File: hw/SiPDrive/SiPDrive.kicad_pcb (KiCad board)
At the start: 8 copper layers, 23 x 27.5 mm, 62 parts, among them Q1 CMSA015N06, Q2 CMSA015N06, Q3 CMSA015N06, Q4 CMSA015N06, Q5 CMSA015N06, Q6 CMSA015N06, U1 STSPIN32G4, U2 MT6701, U3 TCAN1057, U4 LDO, U5 SH-3P

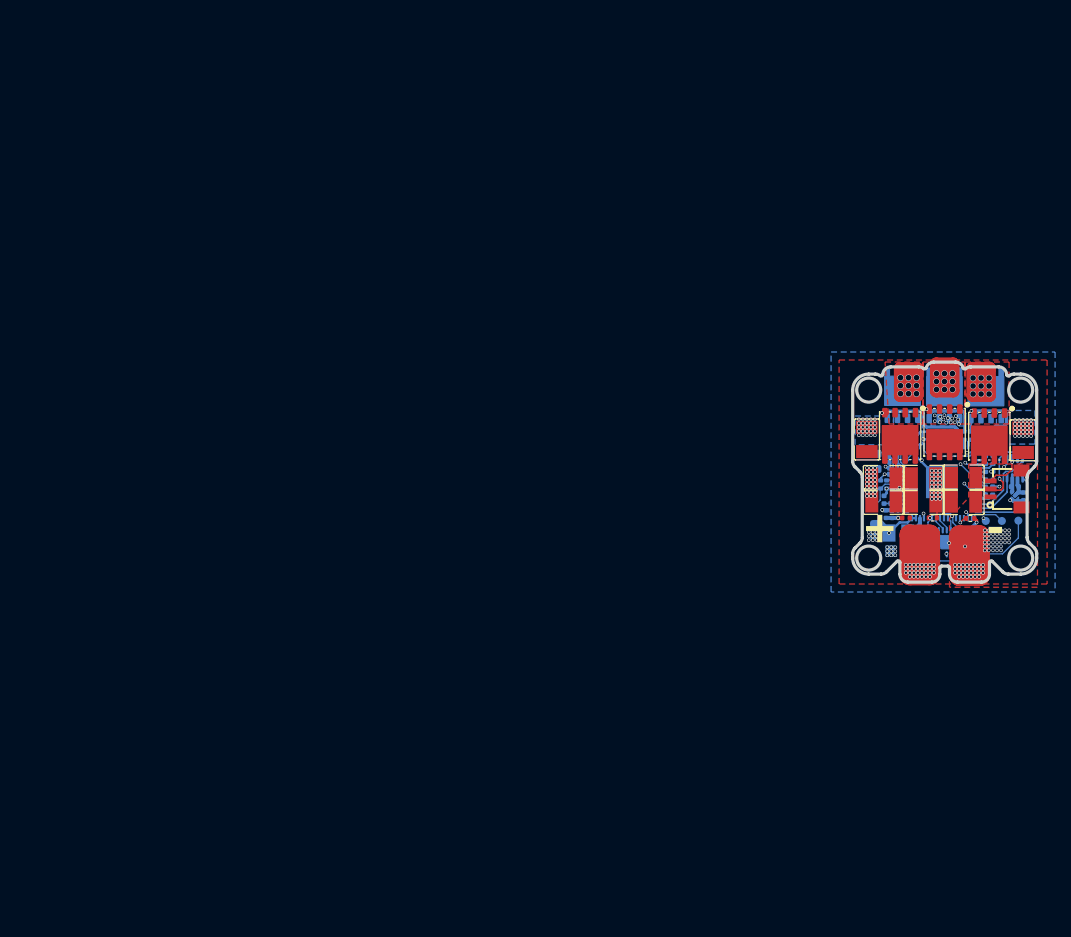
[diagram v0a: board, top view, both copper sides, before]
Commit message: Updated schematic to a 3 shunt topology and made first deboard PCB layout
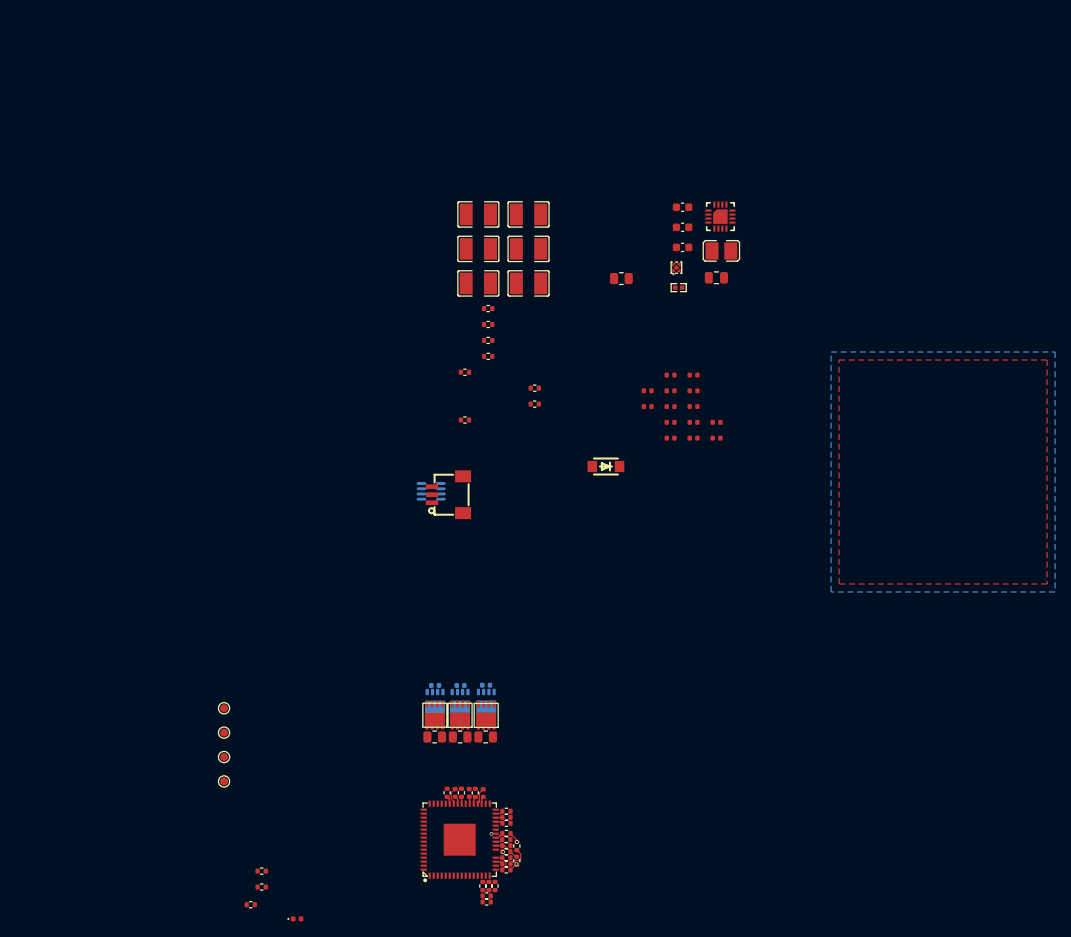
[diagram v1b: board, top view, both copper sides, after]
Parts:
- removed C24, C26: 10uF, SiPDrive:C1210
- added C27: 1uF, Capacitor_SMD:C_0402_1005Metric, B.Cu at (92.9, 125.7)
- added C28: 1uF, Capacitor_SMD:C_0402_1005Metric, B.Cu at (86.5, 125.7)
- added C29: 1uF, Capacitor_SMD:C_0402_1005Metric, B.Cu at (89.7, 125.7)
- added C30: 33n, Capacitor_SMD:C_0402_1005Metric, F.Cu at (121.7, 92.8)
- added C31: 1uF, Capacitor_SMD:C_0603_1608Metric, F.Cu at (117.4, 70.9)
- added C8: 100n, Capacitor_SMD:C_0402_1005Metric, F.Cu at (115.9, 88.9)
- added R20: 1mR, Resistor_SMD:R_0805_2012Metric, F.Cu at (86.5, 132.1)
- added R21: 120R, Resistor_SMD:R_0805_2012Metric, F.Cu at (109.8, 74.8)
- added R22: 1.5k, Resistor_SMD:R_0402_1005Metric, F.Cu at (92.5, 150.8)
- added R23: 1.5k, Resistor_SMD:R_0402_1005Metric, F.Cu at (93.2, 150.8)
- added R24: 15k, Resistor_SMD:R_0402_1005Metric, F.Cu at (94.0, 150.8)
- added R25: 30k, Resistor_SMD:R_0402_1005Metric, F.Cu at (93.0, 152.0)
- added R26: 30k, Resistor_SMD:R_0402_1005Metric, F.Cu at (93.0, 152.8)
- added R27: 15k, Resistor_SMD:R_0402_1005Metric, F.Cu at (95.4, 144.9)
- added R28: 1.5k, Resistor_SMD:R_0402_1005Metric, F.Cu at (95.4, 145.7)
- added R29: 1.5k, Resistor_SMD:R_0402_1005Metric, F.Cu at (95.4, 144.2)
- added R30: 30k, Resistor_SMD:R_0402_1005Metric, F.Cu at (96.7, 147.6)
- added R31: 30k, Resistor_SMD:R_0402_1005Metric, F.Cu at (95.4, 146.5)
- added R32: 15k, Resistor_SMD:R_0402_1005Metric, F.Cu at (95.4, 148.0)
- added R33: 1.5k, Resistor_SMD:R_0402_1005Metric, F.Cu at (95.4, 147.2)
- added R34: 1.5k, Resistor_SMD:R_0402_1005Metric, F.Cu at (96.7, 145.8)
- added R35: 30k, Resistor_SMD:R_0402_1005Metric, F.Cu at (95.4, 148.7)
- added R36: 30k, Resistor_SMD:R_0402_1005Metric, F.Cu at (99.0, 88.5)
- added R37: 10k, Resistor_SMD:R_0402_1005Metric, F.Cu at (99.0, 90.5)
- C1, C10, C11, C12, C13, C14, C15, C16, C17, C2, C3, C4, C5, C6, C9, D1, D2, FB1, L1, R11, R12, R13, R14, R16, R18, R2, R3, R4, R5, R6, R7, R8, R9, TP1, TP2, TP3, TP4, U1, U2, U4: moved to F.Cu
- C7: value 100n -> 220n; footprint Capacitor_SMD:C_0402_1005Metric -> Capacitor_SMD:C_0603_1608Metric
- Q1, Q3, Q5: value CMSA015N06 -> SP40N03GNJ; footprint SiPDrive:PDFN-8_L5.8-W5.0-P1.27-LS6.1-BL -> SiPDrive:POWERPAK-1212-8_L3.0-W3.0-P0.65-LS3.3-BL; moved to B.Cu
- Q2, Q4, Q6: value CMSA015N06 -> SP40N03GNJ; footprint SiPDrive:PDFN-8_L5.8-W5.0-P1.27-LS6.1-BL -> SiPDrive:POWERPAK-1212-8_L3.0-W3.0-P0.65-LS3.3-BL; moved to F.Cu
- R1, R19: value HOSRX -> 1mR; footprint SiPDrive:RES-SMD_L3.2-W1.6_SR120620F0M50SZ -> Resistor_SMD:R_0805_2012Metric; moved to F.Cu
- R10: value 200k -> 100k; moved to F.Cu
- R15: value 10k -> 100k
- moved TP4 104.5 mm to (60.1, 137.7), turned to 0 degrees
- moved TP2 100.8 mm to (60.1, 131.6), turned to 0 degrees
- moved TP1 98.1 mm to (60.1, 128.5), turned to 0 degrees
- moved R17 94.8 mm to (64.8, 148.9)
- moved R16 94.6 mm to (63.5, 153.1), turned to 0 degrees
- moved R18 92.5 mm to (64.8, 150.9), turned to 0 degrees
- moved D2 90.2 mm to (69.3, 154.9), turned to 0 degrees
- moved TP3 86.8 mm to (60.1, 134.6)
- moved R2 78.0 mm to (88.0, 139.1)
- moved R4 77.4 mm to (89.8, 139.1)
- moved R7 77.0 mm to (91.5, 139.1)
- moved C1 76.3 mm to (89.0, 139.1), turned to 90 degrees
- moved C4 75.8 mm to (90.8, 139.1), turned to 90 degrees
- moved C5 75.4 mm to (92.5, 139.1), turned to 90 degrees
- moved U1 75.0 mm to (89.6, 145.0), turned to 90 degrees
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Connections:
- Q4 pad 3: GND -> Net-(Q4-S)
- R1 pad 2: Net-(Q2-S) -> Net-(Q4-S)
- R6 pad 1: /ENC_MODE -> Net-(JP1-B)
- U1 pad 14: Net-(Q2-S) -> Net-(U1-PA1)
- U1 pad 16: GND -> Net-(U1-PA3)
- U1 pad 18: GND -> unconnected-(U1-PA5-Pad18)
- U1 pad 19: unconnected-(U1-PA6-Pad19) -> Net-(U1-PA6)
- U1 pad 20: Net-(Q6-S) -> Net-(U1-PA7)
- U1 pad 23: unconnected-(U1-PB0-Pad23) -> Net-(U1-PB0)
- U1 pad 56: /ENC_MODE -> unconnected-(U1-PB5-Pad56)
- U2 pad 14: /ENC_MODE -> Net-(JP1-B)
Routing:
- net GND: track 32.3 -> 1.54 mm, vias 205 -> 2
- net +12V: track 25.8 -> 0.00 mm, vias 2 -> 0
- net Net-(Q1-G): track 20.4 -> 0.00 mm, vias 2 -> 0
- net /BOOT0: track 19.3 -> 0.00 mm, vias 1 -> 0
- net +3.3V: track 20.8 -> 1.73 mm, vias 5 -> 2
- net /PhaseU: track 19.0 -> 2.14 mm, vias 10 -> 0
- net /PhaseV: track 14.2 -> 0.00 mm, vias 10 -> 0
- net Net-(Q3-G): track 12.8 -> 0.00 mm, vias 2 -> 0
- net /PhaseW: track 14.1 -> 2.09 mm, vias 10 -> 0
- net Net-(Q2-G): track 11.5 -> 0.00 mm
- net Net-(Q5-G): track 11.1 -> 0.00 mm, vias 1 -> 0
- net /CAN_TX: track 10.0 -> 0.00 mm
- net Net-(Q6-S): track 9.59 -> 0.00 mm
- net /CAN_EN: track 9.33 -> 0.00 mm
- net /ENC_MODE: track 8.96 -> 0.00 mm, vias 2 -> 0
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- removed copper zone on F.Cu, net /PhaseU
- removed copper zone on F.Cu, net /PhaseV
- removed copper zone on F.Cu, net /PhaseW
- removed copper zone on F.Cu, net GND
- removed copper zone on B.Cu, net Net-(Q2-S)
- removed copper zone on B.Cu, net Net-(Q6-S)
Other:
- board outline removed
- board text removed: "+"
- board text removed: "-"
- board text removed: "3S-12S"
- board text removed: "mini"
- board text removed: "moteus"

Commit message: Ordered first dev board and components
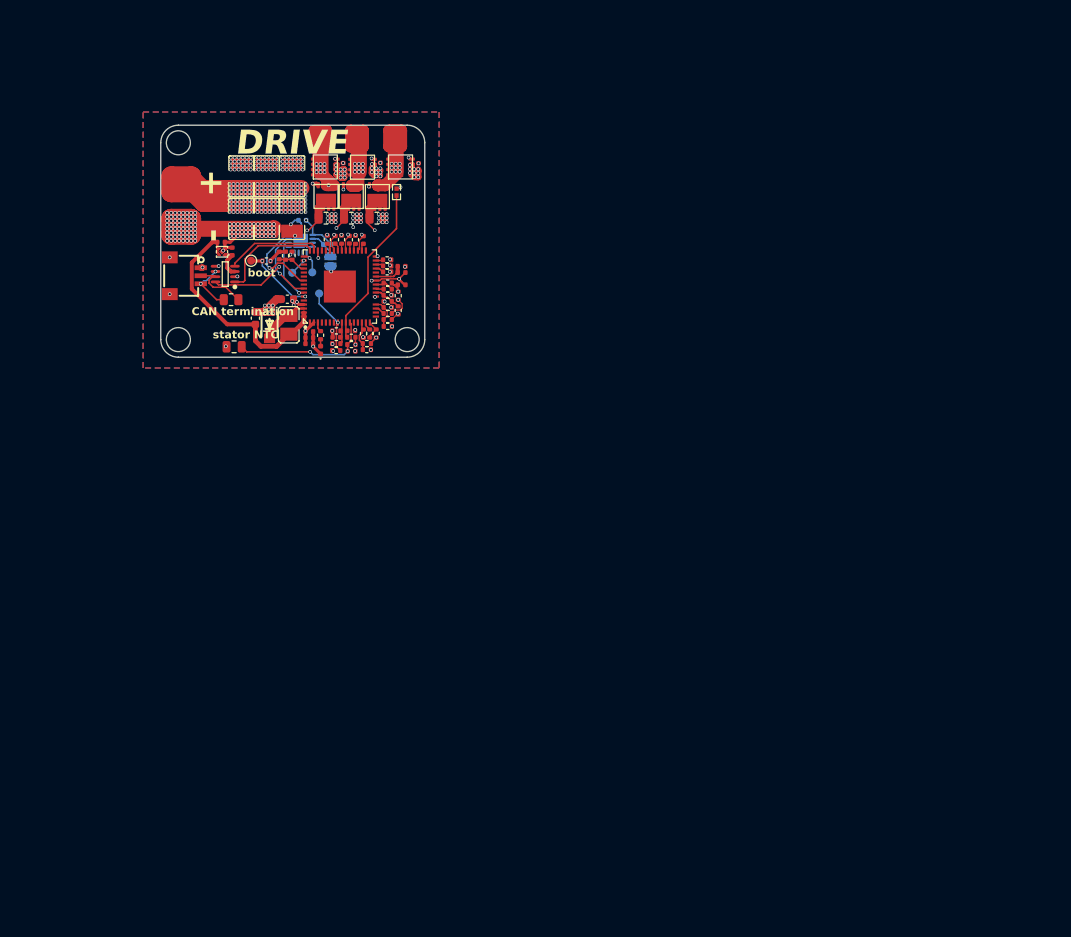
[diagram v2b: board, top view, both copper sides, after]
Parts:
- removed C3, C8: 100n, Capacitor_SMD:C_0402_1005Metric
- added JP1: jmpOpen1, Jumper:SolderJumper-2_P1.3mm_Open_RoundedPad1.0x1.5mm, B.Cu at (73.4, 72.7)
- C12, R6, TP1, TP2, TP3, U2: moved to B.Cu
- C27, C28, C29, Q1, Q3, Q5, U3: moved to F.Cu
- C31: footprint Capacitor_SMD:C_0603_1608Metric -> Capacitor_SMD:C_0402_1005Metric
- moved R17 76.3 mm to (65.4, 72.6)
- moved D2 71.2 mm to (72.2, 83.8), turned to 90 degrees
- moved R24 70.8 mm to (78.3, 81.7)
- moved C1 70.7 mm to (74.0, 70.0)
- moved C4 70.7 mm to (75.8, 70.0)
- moved R7 70.7 mm to (76.5, 70.0)
- moved U1 70.7 mm to (74.6, 75.8)
- moved R2 70.7 mm to (73.0, 70.0)
- moved R4 70.7 mm to (74.8, 70.0)
- moved C5 70.7 mm to (77.5, 70.0)
- moved R25 70.7 mm to (78.0, 82.9)
- moved R26 70.7 mm to (78.0, 83.7)
- moved R22 70.6 mm to (77.5, 81.7)
- moved R3 70.5 mm to (80.5, 74.0)
- moved R5 70.5 mm to (80.5, 73.2)
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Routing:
- net +BATT: track 0.00 -> 65.6 mm, vias 0 -> 191
- net GND: track 1.54 -> 42.2 mm, vias 2 -> 249
- net +12V: track 0.00 -> 29.8 mm
- net Net-(Q2-S): track 0.00 -> 21.1 mm, vias 0 -> 2
- net /BOARD_NTC: track 0.00 -> 20.4 mm
- net Net-(Q4-S): track 0.00 -> 19.2 mm, vias 0 -> 2
- net Net-(Q2-G): track 0.00 -> 18.8 mm, vias 0 -> 2
- net /PhaseW: track 2.09 -> 20.4 mm, vias 0 -> 10
- net /PhaseV: track 0.00 -> 17.9 mm, vias 0 -> 10
- net Net-(Q4-G): track 0.00 -> 17.7 mm, vias 0 -> 2
- net /STATOR_NTC: track 0.00 -> 17.7 mm, vias 0 -> 2
- net +3.3V: track 1.73 -> 18.3 mm, vias 2 -> 10
- net /PhaseU: track 2.14 -> 17.5 mm, vias 0 -> 11
- net /CAN_EN: track 0.00 -> 15.4 mm, vias 0 -> 2
- net Net-(Q6-S): track 0.00 -> 15.2 mm, vias 0 -> 2
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- added copper zone on In5.Cu, net +3.3V
- added copper zone on In1.Cu, net +BATT
- added copper zone on F.Cu, net GND
- removed copper zone on In3.Cu, net +3.3V
- removed copper zone on F.Cu, net +BATT
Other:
- board outline added: 33 x 29 mm
- board text added: "+"
- board text added: "-"
- board text added: "CAN termination"
- board text added: "CLK"
- board text added: "DRIVE"
- board text added: "NRST"
- board text added: "SIP"
- board text added: "boot"
- board text added: "mode select"
- board text added: "stator NTC"
- board text added: "swd"

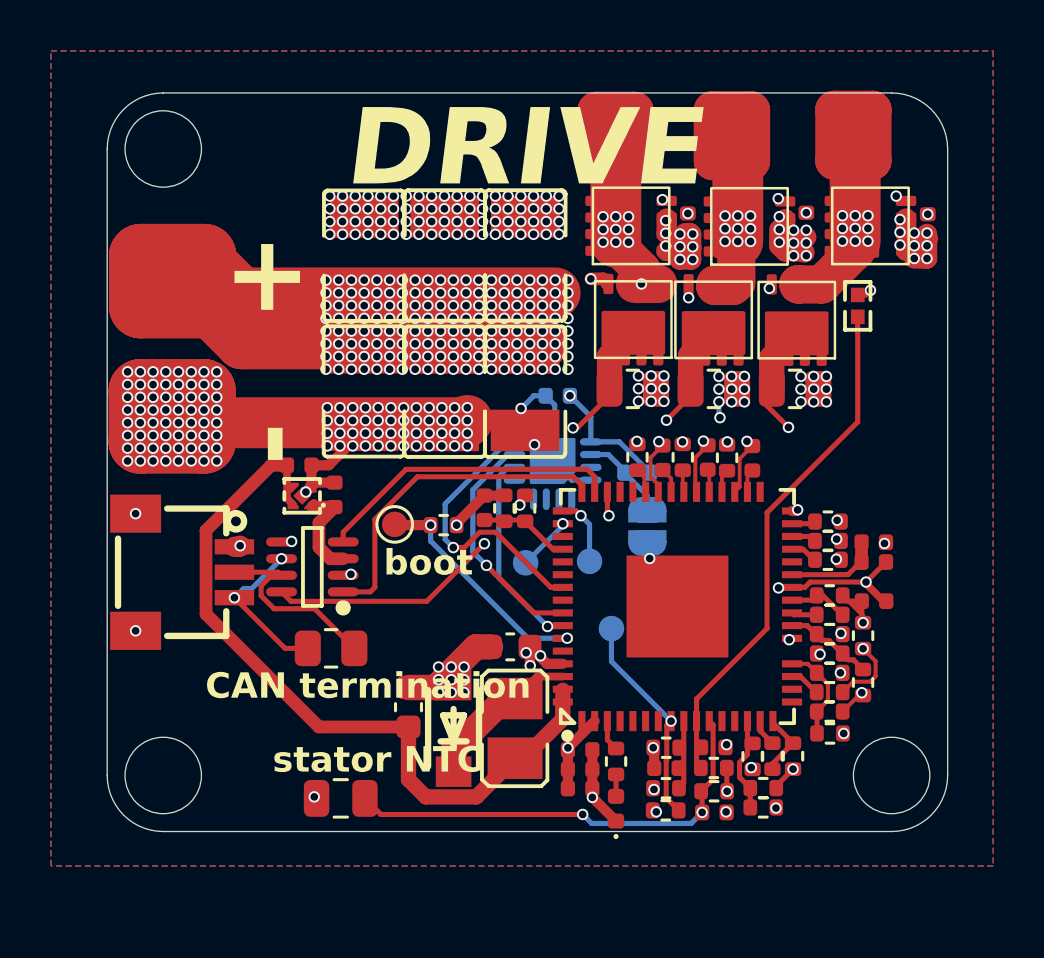
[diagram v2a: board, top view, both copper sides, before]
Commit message: other shunts, redo routing
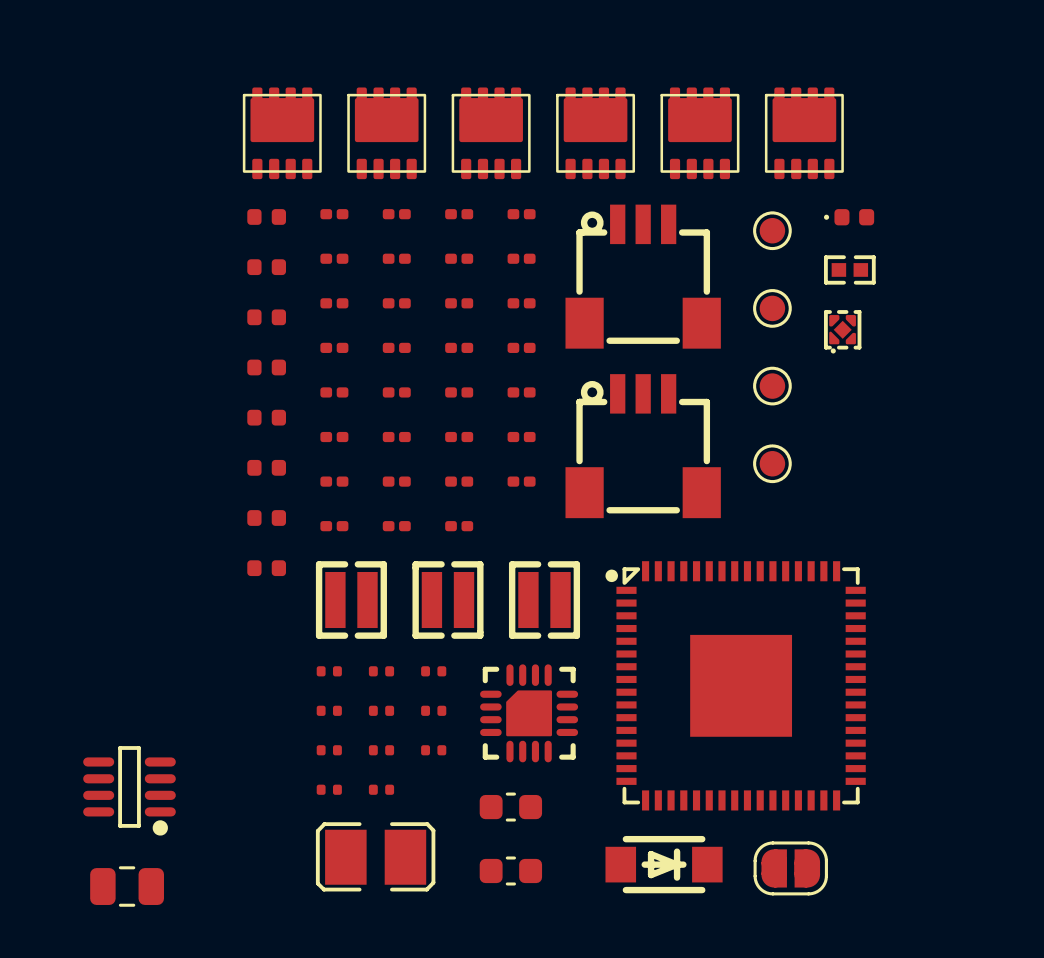
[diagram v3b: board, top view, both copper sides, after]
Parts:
- removed C18, C19, C20, C21, C22, C23: 10uF, SiPDrive:C1210
- removed R20: 1mR, Resistor_SMD:R_0805_2012Metric
- added U6: SH-3P, SiPDrive:CONN-SMD_SM03B-SRSS-TB-LF-SN-P, F.Cu at (73.3, 69.4)
- C1, C10, C14, C15, C16, C2, C30, C4, C5, C6: footprint Capacitor_SMD:C_0402_1005Metric -> Capacitor_SMD:C_0201_0603Metric
- C12: footprint Capacitor_SMD:C_0402_1005Metric -> Capacitor_SMD:C_0201_0603Metric; moved to F.Cu
- JP1, TP1, TP2, TP3, U2: moved to F.Cu
- R1, R19: value 1mR -> SME08A1FR002T; footprint Resistor_SMD:R_0805_2012Metric -> SiPDrive:R0508
- R10, R11, R13, R15, R16, R17, R18, R2, R22, R23, R24, R25, R26, R27, R28, R29, R3, R30, R31, R32, R33, R34, R35, R36, R37, R4, R5, R7, R8, R9: footprint Resistor_SMD:R_0402_1005Metric -> Resistor_SMD:R_0201_0603Metric
- R21: value 120R -> SME08A1FR002T; footprint Resistor_SMD:R_0805_2012Metric -> SiPDrive:R0508
- R6: footprint Resistor_SMD:R_0402_1005Metric -> Resistor_SMD:R_0201_0603Metric; moved to F.Cu
- moved C27 26.5 mm to (58.5, 66.4), turned to 0 degrees
- moved D2 25.0 mm to (81.5, 60.5), turned to 0 degrees
- moved R23 25.0 mm to (66.0, 60.4), turned to 0 degrees
- moved C11 24.9 mm to (58.5, 60.5)
- moved R10 24.9 mm to (63.6, 60.4), turned to 0 degrees
- moved C31 23.9 mm to (58.5, 72.3)
- moved FB1 23.8 mm to (58.5, 74.3), turned to 0 degrees
- moved R11 23.6 mm to (63.6, 62.2)
- moved C29 23.2 mm to (58.5, 70.4), turned to 0 degrees
- moved R24 23.1 mm to (66.0, 62.2), turned to 0 degrees
- moved R13 22.9 mm to (63.6, 63.9)
- moved R3 22.7 mm to (61.1, 62.2)
- moved R25 22.5 mm to (66.0, 63.9)
- moved U4 22.2 mm to (81.1, 65.0), turned to 0 degrees
- moved C2 21.8 mm to (60.9, 79.9), turned to 0 degrees
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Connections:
- R21 pad 1: /CAN_H -> GND
- R21 pad 2: /CAN_L -> Net-(Q2-S)
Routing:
- net +BATT: track 65.6 -> 0.00 mm, vias 191 -> 0
- net GND: track 42.2 -> 0.00 mm, vias 249 -> 0
- net +12V: track 29.8 -> 0.00 mm
- net Net-(Q2-S): track 21.1 -> 0.00 mm, vias 2 -> 0
- net /BOARD_NTC: track 20.4 -> 0.00 mm
- net /PhaseW: track 20.4 -> 0.00 mm, vias 10 -> 0
- net Net-(Q4-S): track 19.2 -> 0.00 mm, vias 2 -> 0
- net Net-(Q2-G): track 18.8 -> 0.00 mm, vias 2 -> 0
- net +3.3V: track 18.3 -> 0.00 mm, vias 10 -> 0
- net /PhaseV: track 17.9 -> 0.00 mm, vias 10 -> 0
- net Net-(Q4-G): track 17.7 -> 0.00 mm, vias 2 -> 0
- net /STATOR_NTC: track 17.7 -> 0.00 mm, vias 2 -> 0
- net /PhaseU: track 17.5 -> 0.00 mm, vias 11 -> 0
- net /CAN_EN: track 15.4 -> 0.00 mm, vias 2 -> 0
- net Net-(Q6-S): track 15.2 -> 0.00 mm, vias 2 -> 0
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- removed copper zone on In5.Cu, net +3.3V
- removed copper zone on In1.Cu, net +BATT
- removed copper zone on B.Cu, net GND
- removed copper zone on F.Cu, net GND
- removed copper zone on In1.Cu, net GND
- removed copper zone on In2.Cu, net GND
- removed copper zone on In3.Cu, net GND
- removed copper zone on In4.Cu, net GND
- removed copper zone on In5.Cu, net GND
- removed copper zone on In6.Cu, net GND
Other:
- board outline removed
- board text removed: "+"
- board text removed: "-"
- board text removed: "CAN termination"
- board text removed: "CLK"
- board text removed: "DRIVE"
- board text removed: "NRST"
- board text removed: "SIP"
- board text removed: "boot"
- board text removed: "mode select"
- board text removed: "stator NTC"
- board text removed: "swd"
